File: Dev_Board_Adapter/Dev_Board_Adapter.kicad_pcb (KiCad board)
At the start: 2 copper layers, 37 x 38 mm, 4 parts, among them J1 HARWIN_KALMAN, J2 Conn_02x10_Odd_Even, J3 Conn_01x03_Male, J4 Conn_01x08_Male

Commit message: fix spacing
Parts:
- moved J4 6.36 mm to (117.1, 94.5)
- moved J2 2.31 mm to (126.0, 71.7)
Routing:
- net +5V: track 34.9 -> 24.8 mm
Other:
- board size 37 x 38 mm -> 24.7 x 31.1 mm
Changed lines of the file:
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@@
   (setup
     (pad_to_mask_clearance 0)
+    (grid_origin 129.54 73.406)
     (pcbplotparams
       (layerselection 0x00010fc_ffffffff)
@@
   (net 31 "/CAN_PAYLOAD+")
   (footprint "Connector_PinHeader_2.54mm:PinHeader_1x08_P2.54mm_Vertical" (layer "F.Cu")
-    (at 112.014 90.678 180)
+    (at 117.0686 94.5388 180)
     (descr "Through hole straight pin header, 1x08, 2.54mm pitch, single row")
     (tags "Through hole pin header THT 1x08 2.54mm single row")
@@
   )
   (footprint "Connector_PinHeader_2.54mm:PinHeader_2x10_P2.54mm_Vertical" (layer "B.Cu")
-    (at 123.698 72.136 180)
+    (at 125.9586 71.6788 180)
     (descr "Through hole straight pin header, 2x10, 2.54mm pitch, double rows")
     (tags "Through hole pin header THT 2x10 2.54mm double row")
@@
     )
   )
-  (gr_rect locked (start 100 70) (end 137 108) (layer "Edge.Cuts") (width 0.1) (fill none))
-  (segment (start 118.364 97.79) (end 119.634 99.06) (width 1) (layer "F.Cu") (net 22))
-  (segment (start 127.762 90.424) (end 130.064 90.424) (width 1) (layer "F.Cu") (net 22))
-  (segment (start 126.746 91.44) (end 127.762 90.424) (width 1) (layer "F.Cu") (net 22))
-  (segment (start 118.364 89.154) (end 118.364 97.79) (width 1) (layer "F.Cu") (net 22))
-  (segment (start 117.348 88.138) (end 118.364 89.154) (width 1) (layer "F.Cu") (net 22))
-  (segment (start 112.014 88.138) (end 117.348 88.138) (width 1) (layer "F.Cu") (net 22))
-  (segment (start 126.746 97.79) (end 126.746 91.44) (width 1) (layer "F.Cu") (net 22))
-  (segment (start 125.476 99.06) (end 126.746 97.79) (width 1) (layer "F.Cu") (net 22))
-  (segment (start 119.634 99.06) (end 125.476 99.06) (width 1) (layer "F.Cu") (net 22))
+  (gr_rect (start 112.268 70) (end 137 101.092) (layer "Edge.Cuts") (width 0.1) (fill none))
+  (dimension (type orthogonal) (layer "User.1")
+    (pts (xy 129.54 73.406) (xy 125.984 76.708))
+    (height -7.874)
+    (orientation 0)
+    (gr_text "3.5560 mm" (at 134.62 65.532) (layer "User.1")
+      (effects (font (size 1 1) (thickness 0.15)))
+    )
+    (format (units 3) (units_format 1) (precision 4))
+    (style (thickness 0.15) (arrow_length 1.27) (text_position_mode 2) (extension_height 0.58642) (extension_offset 0.5) keep_text_aligned)
+  )
+  (dimension (type orthogonal) (layer "User.1")
+    (pts (xy 117.094 91.948) (xy 129.54 73.406))
+    (height -29.718)
+    (orientation 0)
+    (gr_text "12.4460 mm" (at 123.444 60.96) (layer "User.1")
+      (effects (font (size 1 1) (thickness 0.15)))
+    )
+    (format (units 3) (units_format 1) (precision 4))
+    (style (thickness 0.15) (arrow_length 1.27) (text_position_mode 2) (extension_height 0.58642) (extension_offset 0.5) keep_text_aligned)
+  )
+  (dimension (type orthogonal) (layer "User.1")
+    (pts (xy 129.54 73.406) (xy 123.4186 94.5388))
+    (height -22.098)
+    (orientation 1)
+    (gr_text "21.1328 mm" (at 105.918 84.582 90) (layer "User.1")
+      (effects (font (size 1 1) (thickness 0.15)))
+    )
+    (format (units 3) (units_format 1) (precision 4))
+    (style (thickness 0.15) (arrow_length 1.27) (text_position_mode 2) (extension_height 0.58642) (extension_offset 0.5) keep_text_aligned)
+  )
+  (segment (start 128.27 97.536) (end 128.27 92.218) (width 1) (layer "F.Cu") (net 22))
+  (segment (start 127.508 98.298) (end 128.27 97.536) (width 1) (layer "F.Cu") (net 22))
+  (segment (start 120.396 92.964) (end 120.396 97.79) (width 1) (layer "F.Cu") (net 22))
+  (segment (start 117.0686 91.9988) (end 119.4308 91.9988) (width 1) (layer "F.Cu") (net 22))
+  (segment (start 128.27 92.218) (end 130.064 90.424) (width 1) (layer "F.Cu") (net 22))
+  (segment (start 119.4308 91.9988) (end 120.396 92.964) (width 1) (layer "F.Cu") (net 22))
+  (segment (start 120.904 98.298) (end 127.508 98.298) (width 1) (layer "F.Cu") (net 22))
+  (segment (start 120.396 97.79) (end 120.904 98.298) (width 1) (layer "F.Cu") (net 22))
   (segment (start 134.845 87.643) (end 134.845 79.6628) (width 0.2) (layer "F.Cu") (net 30))
   (segment (start 132.559 75.975) (end 132.588 75.946) (width 0.2) (layer "F.Cu") (net 30))
@@
     (polygon
       (pts
-        (xy 137.922 109.474)
-        (xy 98.552 109.474)
-        (xy 98.806 68.072)
-        (xy 137.922 68.072)
+        (xy 137.668 101.6)
+        (xy 111.76 101.6)
+        (xy 111.76 69.088)
+        (xy 137.668 69.342)
       )
     )

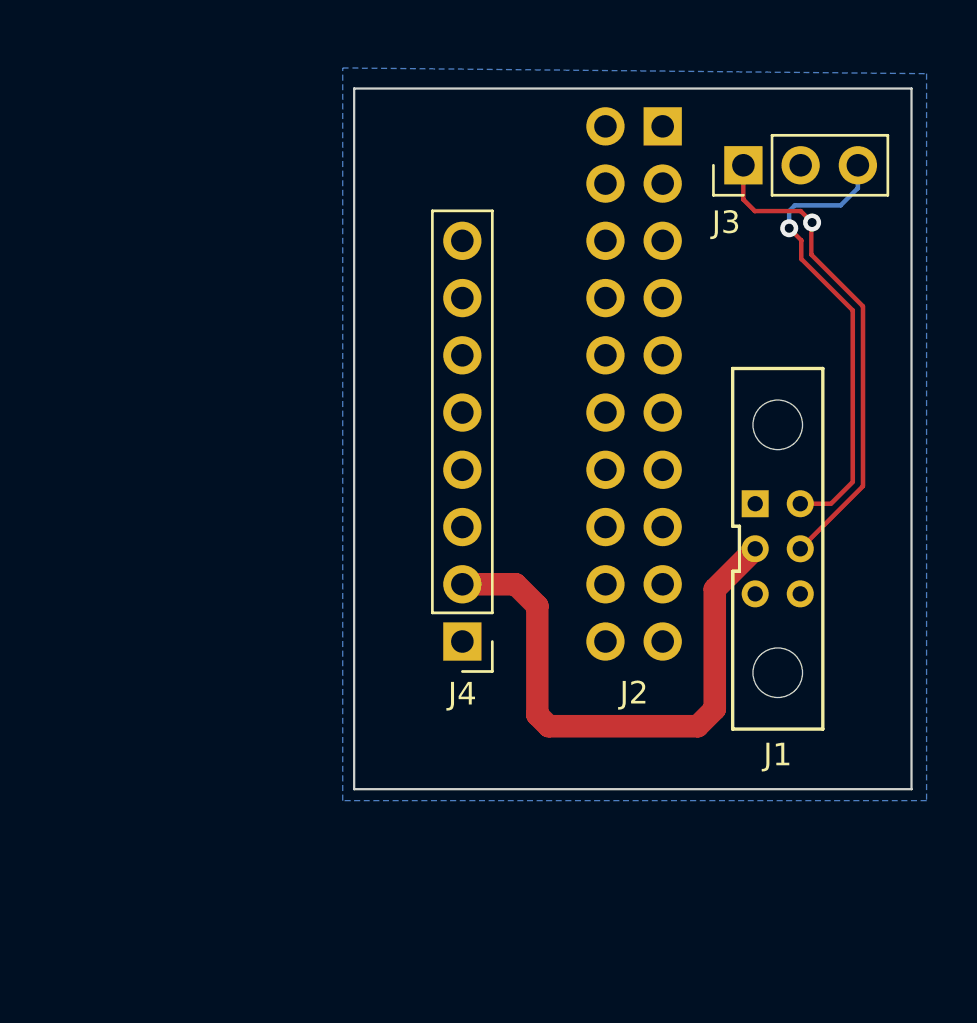
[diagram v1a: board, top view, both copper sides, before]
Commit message: fix edge cuts
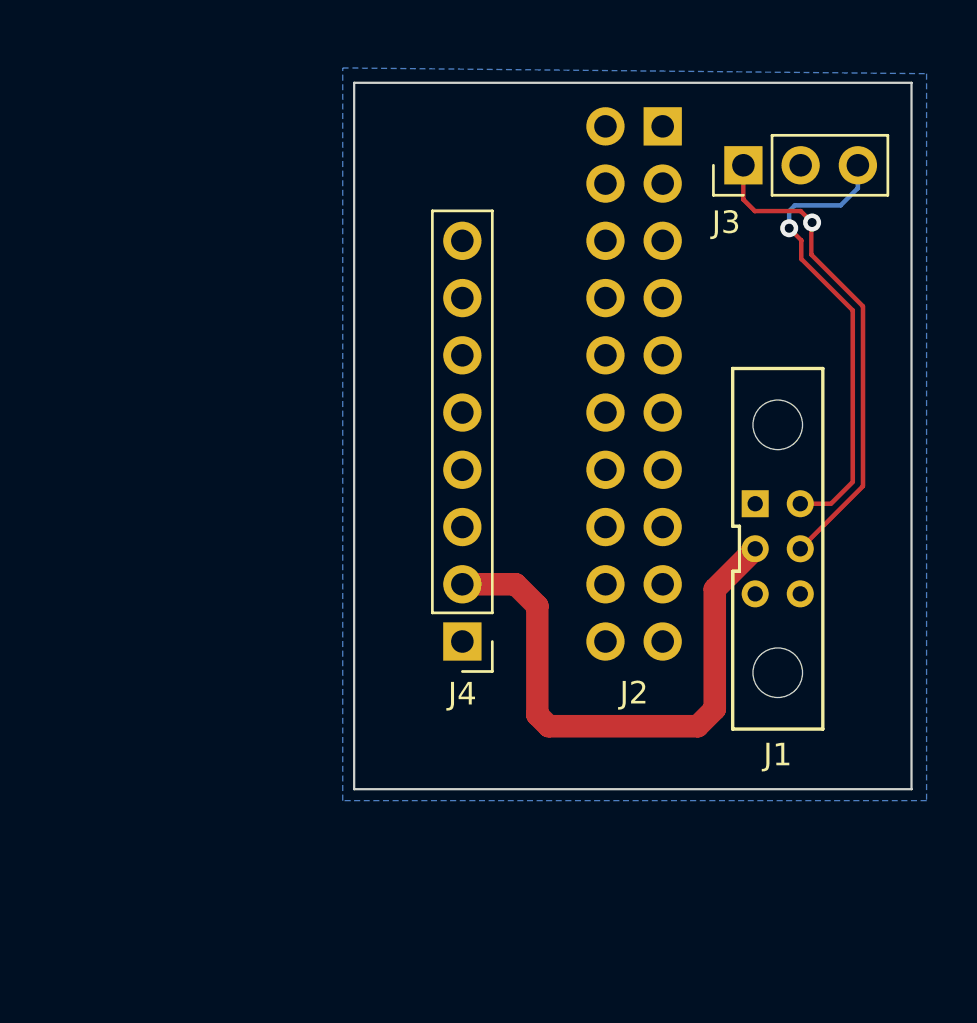
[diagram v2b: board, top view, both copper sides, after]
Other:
- board size 24.7 x 31.1 mm -> 24.7 x 31.3 mm
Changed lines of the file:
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@@
     )
   )
-  (gr_rect (start 112.268 70) (end 137 101.092) (layer "Edge.Cuts") (width 0.1) (fill none))
+  (gr_rect (start 112.268 69.746) (end 137 101.092) (layer "Edge.Cuts") (width 0.1) (fill none))
   (dimension (type orthogonal) (layer "User.1")
     (pts (xy 129.54 73.406) (xy 125.984 76.708))

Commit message: Cleanup spacing, edges, corners
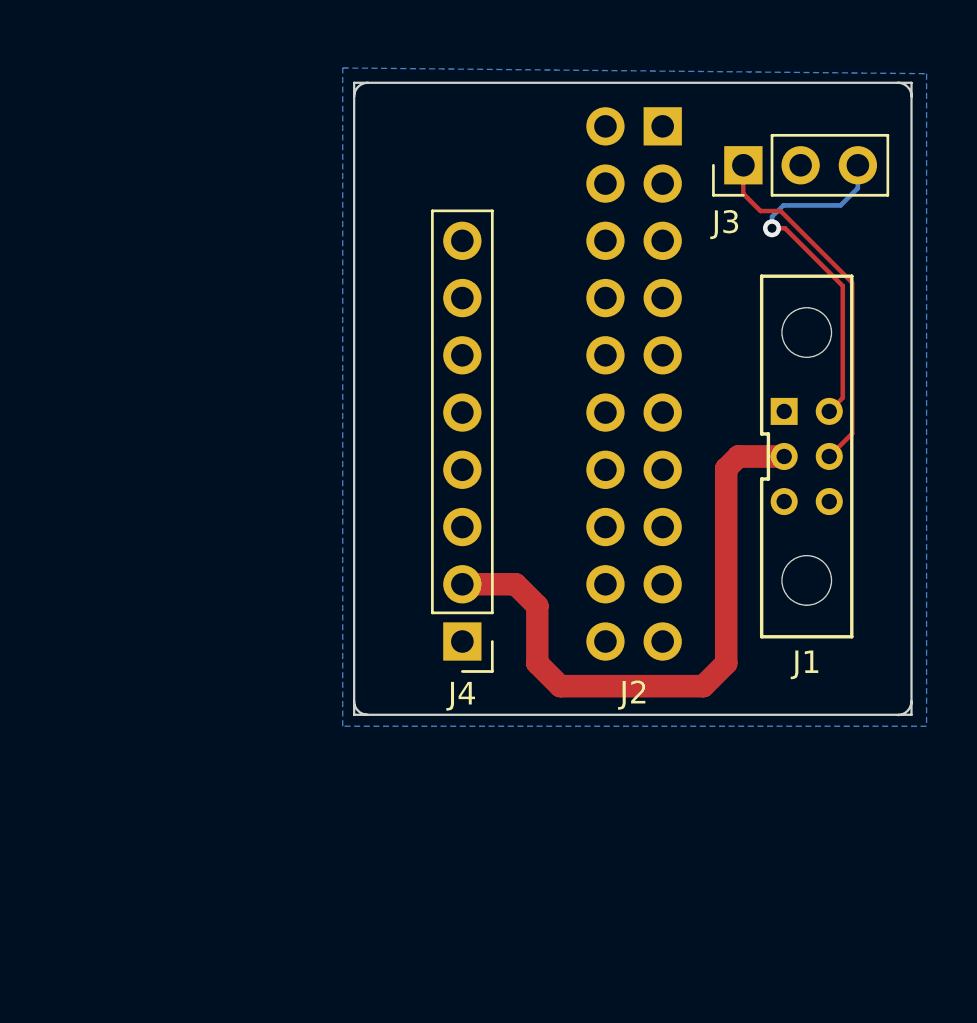
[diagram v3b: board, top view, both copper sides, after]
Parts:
- moved J1 4.29 mm to (132.3, 86.3)
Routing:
- net /CAN_PAYLOAD-: track 21.6 -> 15.9 mm, vias 1 -> 0
- net /CAN_PAYLOAD+: track 20.4 -> 15.9 mm
- net +5V: track 24.8 -> 26.9 mm
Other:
- board size 24.7 x 31.3 mm -> 24.7 x 28.1 mm
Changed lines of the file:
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@@
   )
   (footprint "Dev_Board_Adpater:connector_Harwin_M80-5000642" (layer "F.Cu")
-    (at 131.064 90.424 -90)
+    (at 132.35 86.328 -90)
     (property "Sheetfile" "Dev_Board_Adapter.kicad_sch")
     (property "Sheetname" "")
@@
     )
   )
-  (gr_rect (start 112.268 69.746) (end 137 101.092) (layer "Edge.Cuts") (width 0.1) (fill none))
+  (gr_rect (start 112.268 69.746) (end 137 97.79) (layer "Edge.Cuts") (width 0.1) (fill none))
+  (gr_arc (start 112.267681 70.358006) (mid 112.446932 69.925257) (end 112.879681 69.746006) (layer "Edge.Cuts") (width 0.1))
+  (gr_arc (start 136.390823 69.744194) (mid 136.823572 69.923445) (end 137.002823 70.356194) (layer "Edge.Cuts") (width 0.1))
+  (gr_arc (start 136.994633 97.191375) (mid 136.815382 97.624124) (end 136.382633 97.803375) (layer "Edge.Cuts") (width 0.1))
+  (gr_arc (start 112.874434 97.789677) (mid 112.441685 97.610426) (end 112.262434 97.177677) (layer "Edge.Cuts") (width 0.1))
   (dimension (type orthogonal) (layer "User.1")
     (pts (xy 129.54 73.406) (xy 125.984 76.708))
@@
     (style (thickness 0.15) (arrow_length 1.27) (text_position_mode 2) (extension_height 0.58642) (extension_offset 0.5) keep_text_aligned)
   )
-  (segment (start 128.27 97.536) (end 128.27 92.218) (width 1) (layer "F.Cu") (net 22))
-  (segment (start 127.508 98.298) (end 128.27 97.536) (width 1) (layer "F.Cu") (net 22))
-  (segment (start 120.396 92.964) (end 120.396 97.79) (width 1) (layer "F.Cu") (net 22))
+  (segment (start 128.778 86.868) (end 129.318 86.328) (width 1) (layer "F.Cu") (net 22))
+  (segment (start 120.396 95.504) (end 121.412 96.52) (width 1) (layer "F.Cu") (net 22))
+  (segment (start 128.778 95.504) (end 128.778 86.868) (width 1) (layer "F.Cu") (net 22))
   (segment (start 117.0686 91.9988) (end 119.4308 91.9988) (width 1) (layer "F.Cu") (net 22))
-  (segment (start 128.27 92.218) (end 130.064 90.424) (width 1) (layer "F.Cu") (net 22))
+  (segment (start 120.396 92.964) (end 120.396 95.504) (width 1) (layer "F.Cu") (net 22))
   (segment (start 119.4308 91.9988) (end 120.396 92.964) (width 1) (layer "F.Cu") (net 22))
-  (segment (start 120.904 98.298) (end 127.508 98.298) (width 1) (layer "F.Cu") (net 22))
-  (segment (start 120.396 97.79) (end 120.904 98.298) (width 1) (layer "F.Cu") (net 22))
-  (segment (start 134.845 87.643) (end 134.845 79.6628) (width 0.2) (layer "F.Cu") (net 30))
-  (segment (start 132.559 75.975) (end 132.588 75.946) (width 0.2) (layer "F.Cu") (net 30))
-  (segment (start 129.54 74.93) (end 129.54 73.406) (width 0.2) (layer "F.Cu") (net 30))
-  (segment (start 130.048 75.438) (end 129.54 74.93) (width 0.2) (layer "F.Cu") (net 30))
-  (segment (start 134.845 79.6628) (end 132.559 77.3768) (width 0.2) (layer "F.Cu") (net 30))
-  (segment (start 132.064 90.424) (end 134.845 87.643) (width 0.2) (layer "F.Cu") (net 30))
-  (segment (start 132.588 75.946) (end 132.08 75.438) (width 0.2) (layer "F.Cu") (net 30))
-  (segment (start 132.559 77.3768) (end 132.559 75.975) (width 0.2) (layer "F.Cu") (net 30))
-  (segment (start 132.08 75.438) (end 130.048 75.438) (width 0.2) (layer "F.Cu") (net 30))
-  (via (at 132.588 75.946) (size 0.8) (drill 0.4) (layers "F.Cu" "B.Cu") (free) (net 30))
-  (segment (start 132.064 88.424) (end 133.427603 88.424) (width 0.2) (layer "F.Cu") (net 31))
-  (segment (start 134.395 87.456603) (end 134.395 79.8492) (width 0.2) (layer "F.Cu") (net 31))
-  (segment (start 132.109 76.737) (end 131.572 76.2) (width 0.2) (layer "F.Cu") (net 31))
-  (segment (start 132.109 77.5632) (end 132.109 76.737) (width 0.2) (layer "F.Cu") (net 31))
-  (segment (start 134.395 79.8492) (end 132.109 77.5632) (width 0.2) (layer "F.Cu") (net 31))
-  (segment (start 133.427603 88.424) (end 134.395 87.456603) (width 0.2) (layer "F.Cu") (net 31))
-  (via (at 131.572 76.2) (size 0.8) (drill 0.4) (layers "F.Cu" "B.Cu") (free) (net 31))
+  (segment (start 121.412 96.52) (end 127.762 96.52) (width 1) (layer "F.Cu") (net 22))
+  (segment (start 127.762 96.52) (end 128.778 95.504) (width 1) (layer "F.Cu") (net 22))
+  (segment (start 129.318 86.328) (end 131.35 86.328) (width 1) (layer "F.Cu") (net 22))
+  (segment (start 131.191 75.438) (end 130.302 75.438) (width 0.2) (layer "F.Cu") (net 30))
+  (segment (start 130.302 75.438) (end 129.54 74.676) (width 0.2) (layer "F.Cu") (net 30))
+  (segment (start 134.366 78.613) (end 131.191 75.438) (width 0.2) (layer "F.Cu") (net 30))
+  (segment (start 134.366 85.312) (end 134.366 78.613) (width 0.2) (layer "F.Cu") (net 30))
+  (segment (start 129.54 74.676) (end 129.54 73.406) (width 0.2) (layer "F.Cu") (net 30))
+  (segment (start 133.35 86.328) (end 134.366 85.312) (width 0.2) (layer "F.Cu") (net 30))
+  (segment (start 133.95 78.762006) (end 133.95 83.728) (width 0.2) (layer "F.Cu") (net 31))
+  (segment (start 130.81 76.2) (end 131.387994 76.2) (width 0.2) (layer "F.Cu") (net 31))
+  (segment (start 131.387994 76.2) (end 133.95 78.762006) (width 0.2) (layer "F.Cu") (net 31))
+  (segment (start 133.95 83.728) (end 133.35 84.328) (width 0.2) (layer "F.Cu") (net 31))
+  (via (at 130.81 76.2) (size 0.8) (drill 0.4) (layers "F.Cu" "B.Cu") (free) (net 31))
+  (segment (start 130.81 76.2) (end 130.81 75.692) (width 0.2) (layer "B.Cu") (net 31))
+  (segment (start 131.318 75.184) (end 133.858 75.184) (width 0.2) (layer "B.Cu") (net 31))
+  (segment (start 130.81 75.692) (end 131.318 75.184) (width 0.2) (layer "B.Cu") (net 31))
   (segment (start 133.858 75.184) (end 134.62 74.422) (width 0.2) (layer "B.Cu") (net 31))
-  (segment (start 131.572 76.2) (end 131.572 75.438) (width 0.2) (layer "B.Cu") (net 31))
   (segment (start 134.62 74.422) (end 134.62 73.406) (width 0.2) (layer "B.Cu") (net 31))
-  (segment (start 131.826 75.184) (end 133.858 75.184) (width 0.2) (layer "B.Cu") (net 31))
-  (segment (start 131.572 75.438) (end 131.826 75.184) (width 0.2) (layer "B.Cu") (net 31))
   (zone (net 21) (net_name "GND") (layer "B.Cu") (hatch edge 0.508)
     (connect_pads (clearance 0.508))
@@
     (polygon
       (pts
-        (xy 137.668 101.6)
-        (xy 111.76 101.6)
+        (xy 137.668 98.298)
+        (xy 111.76 98.298)
         (xy 111.76 69.088)
         (xy 137.668 69.342)
